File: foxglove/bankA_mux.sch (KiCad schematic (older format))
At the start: 6 parts, among them U10 SHIFTER, U9 74HC4051

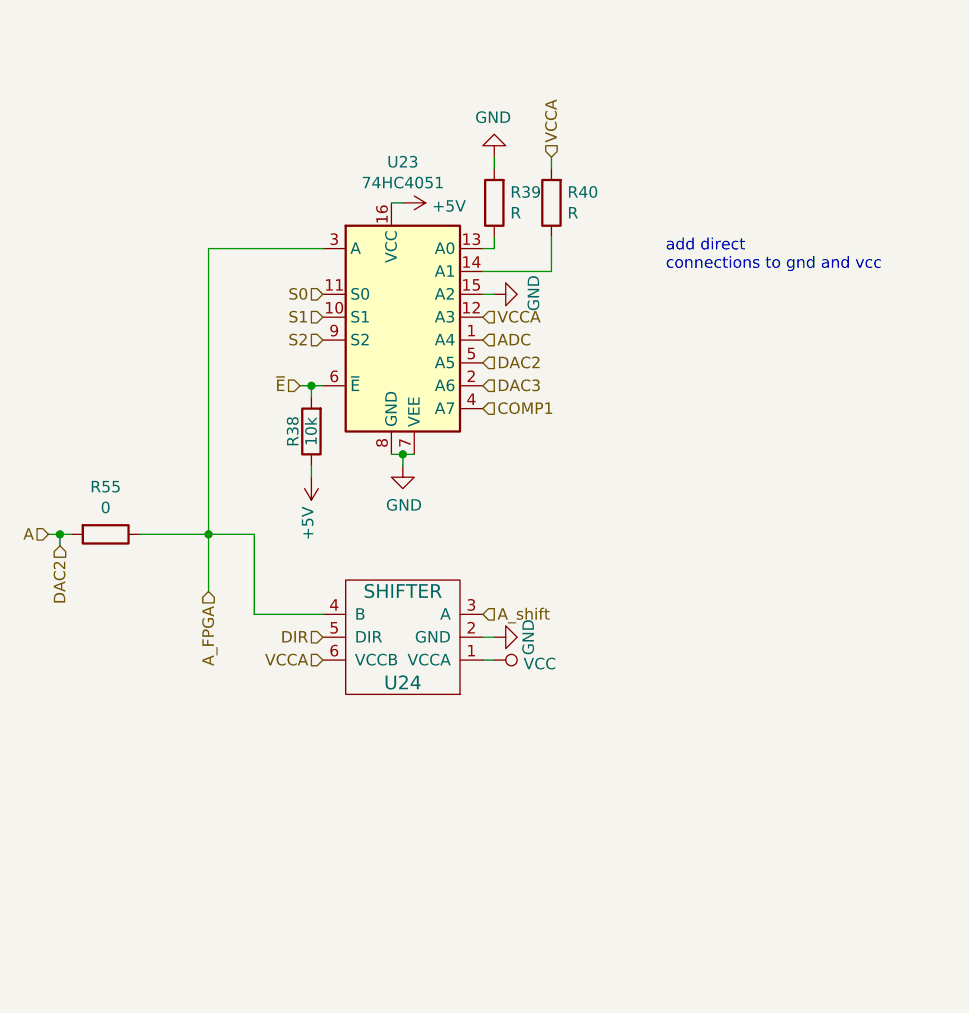
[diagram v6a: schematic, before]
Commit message: Made FPGA connections to greatfet headers
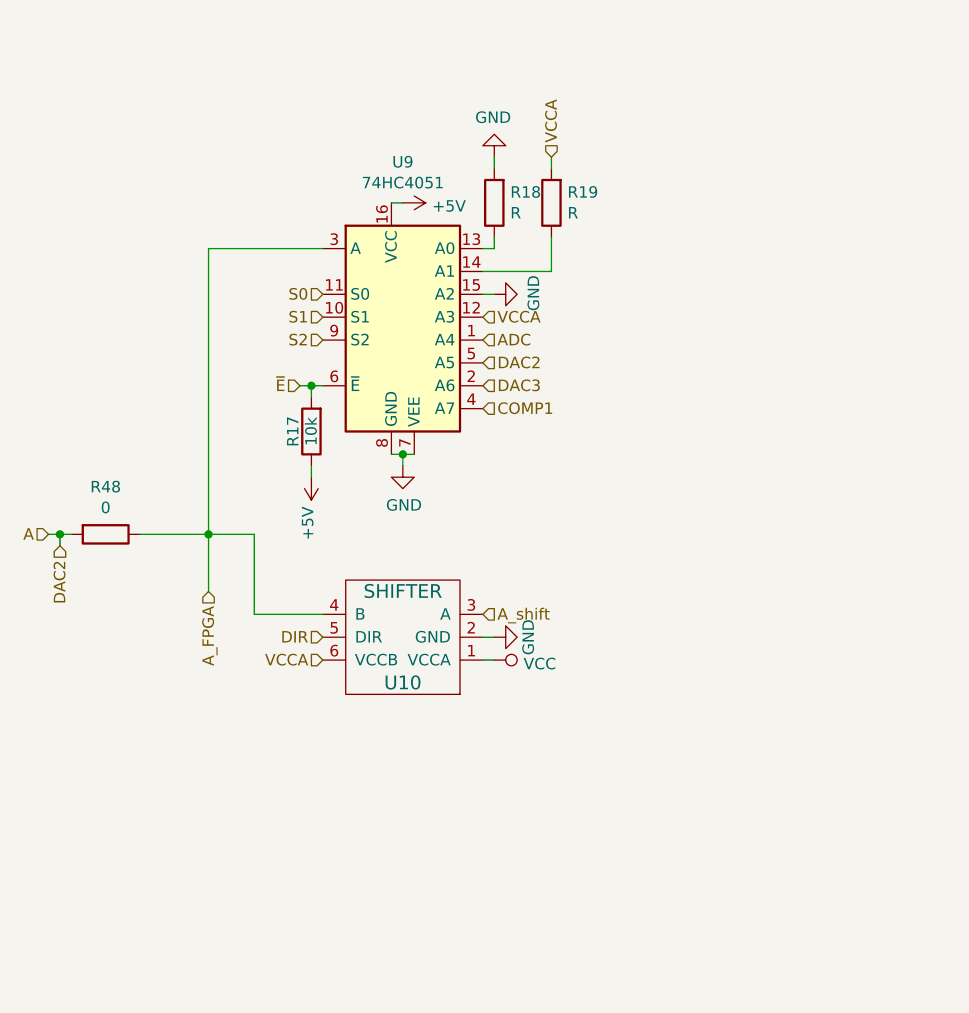
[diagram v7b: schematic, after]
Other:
- note removed: "add direct\nconnections to gnd and vcc"
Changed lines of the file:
@@
 AR Path="/5D1A4680/5CF3E254" Ref="U21"  Part="1"
 AR Path="/5D1A4696/5CF3E254" Ref="U23"  Part="1"
-F 0 "U23" H 4100 3428 50  0000 C CNN
+F 0 "U9" H 4100 3428 50  0000 C CNN
 F 1 "74HC4051" H 4100 3337 50  0000 C CNN
 F 2 "Package_TO_SOT_SMD:SOT-763-1" H 4050 2350 50  0001 C CNN
@@
 AR Path="/5D1A4680/5CF3E25C" Ref="#PWR0180"  Part="1"
 AR Path="/5D1A4696/5CF3E25C" Ref="#PWR0186"  Part="1"
-F 0 "#PWR0186" H 4100 2100 50  0001 C CNN
+F 0 "#PWR0144" H 4100 2100 50  0001 C CNN
 F 1 "+5V" V 4115 2378 50  0000 L CNN
 F 2 "" H 4100 2250 50  0001 C CNN
@@
 AR Path="/5D1A4680/5CF3E263" Ref="#PWR0181"  Part="1"
 AR Path="/5D1A4696/5CF3E263" Ref="#PWR0187"  Part="1"
-F 0 "#PWR0187" H 4100 3150 50  0001 C CNN
+F 0 "#PWR0145" H 4100 3150 50  0001 C CNN
 F 1 "GND" H 4105 3227 50  0000 C CNN
 F 2 "" H 4100 3400 50  0001 C CNN
@@
 AR Path="/5D1A4680/5CF3E26E" Ref="R36"  Part="1"
 AR Path="/5D1A4696/5CF3E26E" Ref="R39"  Part="1"
-F 0 "R39" H 4430 2204 50  0000 R CNN
+F 0 "R18" H 4430 2204 50  0000 R CNN
 F 1 "R" H 4430 2295 50  0000 R CNN
 F 2 "gsg-modules:0402" V 4430 2250 50  0001 C CNN
@@
 AR Path="/5D1A4680/5CF3E275" Ref="R37"  Part="1"
 AR Path="/5D1A4696/5CF3E275" Ref="R40"  Part="1"
-F 0 "R40" H 4680 2204 50  0000 R CNN
+F 0 "R19" H 4680 2204 50  0000 R CNN
 F 1 "R" H 4680 2295 50  0000 R CNN
 F 2 "gsg-modules:0402" V 4680 2250 50  0001 C CNN
@@
 AR Path="/5D1A4680/5CF3E282" Ref="#PWR0182"  Part="1"
 AR Path="/5D1A4696/5CF3E282" Ref="#PWR0188"  Part="1"
-F 0 "#PWR0188" H 4500 1800 50  0001 C CNN
+F 0 "#PWR0146" H 4500 1800 50  0001 C CNN
 F 1 "GND" H 4505 1877 50  0000 C CNN
 F 2 "" H 4500 2050 50  0001 C CNN
@@
 AR Path="/5D1A4680/5CF3E28C" Ref="U22"  Part="1"
 AR Path="/5D1A4696/5CF3E28C" Ref="U24"  Part="1"
-F 0 "U24" H 4100 4350 60  0000 C CNN
+F 0 "U10" H 4100 4350 60  0000 C CNN
 F 1 "SHIFTER" H 4100 3950 60  0000 C CNN
 F 2 "gsg-modules:SOT363" H 4100 4150 60  0001 C CNN
@@
 AR Path="/5D1A4680/5CF3E293" Ref="#PWR0183"  Part="1"
 AR Path="/5D1A4696/5CF3E293" Ref="#PWR0189"  Part="1"
-F 0 "#PWR0189" H 4500 3900 50  0001 C CNN
+F 0 "#PWR0147" H 4500 3900 50  0001 C CNN
 F 1 "GND" H 4500 4000 50  0000 C CNN
 F 2 "" H 4500 4150 60  0000 C CNN
@@
 AR Path="/5D1A4680/5CF3E2A6" Ref="R35"  Part="1"
 AR Path="/5D1A4696/5CF3E2A6" Ref="R38"  Part="1"
-F 0 "R38" V 3780 3250 50  0000 C CNN
+F 0 "R17" V 3780 3250 50  0000 C CNN
 F 1 "10k" V 3700 3250 50  0000 C CNN
 F 2 "gsg-modules:0402" V 3630 3250 50  0001 C CNN
@@
 AR Path="/5D1A4680/5CF3E2B2" Ref="#PWR0184"  Part="1"
 AR Path="/5D1A4696/5CF3E2B2" Ref="#PWR0190"  Part="1"
-F 0 "#PWR0190" H 3700 3300 50  0001 C CNN
+F 0 "#PWR0148" H 3700 3300 50  0001 C CNN
 F 1 "+5V" V 3715 3578 50  0000 L CNN
 F 2 "" H 3700 3450 50  0001 C CNN
@@
 AR Path="/5D1A4680/5CF3E2B8" Ref="#PWR0185"  Part="1"
 AR Path="/5D1A4696/5CF3E2B8" Ref="#PWR0191"  Part="1"
-F 0 "#PWR0191" H 4500 4100 50  0001 C CNN
+F 0 "#PWR0149" H 4500 4100 50  0001 C CNN
 F 1 "VCC" V 4517 4378 50  0000 L CNN
 F 2 "" H 4500 4250 50  0001 C CNN
@@
 AR Path="/5D190D22/5CB0C423" Ref="R51"  Part="1"
 AR Path="/5D1A466A/5CB0C423" Ref="R53"  Part="1"
-F 0 "R55" V 2593 3700 50  0000 C CNN
+F 0 "R48" V 2593 3700 50  0000 C CNN
 F 1 "0" V 2684 3700 50  0000 C CNN
 F 2 "gsg-modules:0402" V 2730 3700 50  0001 C CNN
@@
 Wire Wire Line
 	2950 3700 3250 3700
-Text Notes 5250 2550 0    50   ~ 0
-add direct\nconnections to gnd and vcc
 $Comp
 L power:GND #PWR?
@@
 AR Path="/5D1A4680/5CCD056F" Ref="#PWR0238"  Part="1"
 AR Path="/5D1A4696/5CCD056F" Ref="#PWR0239"  Part="1"
-F 0 "#PWR0239" H 4500 2400 50  0001 C CNN
+F 0 "#PWR0232" H 4500 2400 50  0001 C CNN
 F 1 "GND" H 4505 2477 50  0000 C CNN
 F 2 "" H 4500 2650 50  0001 C CNN

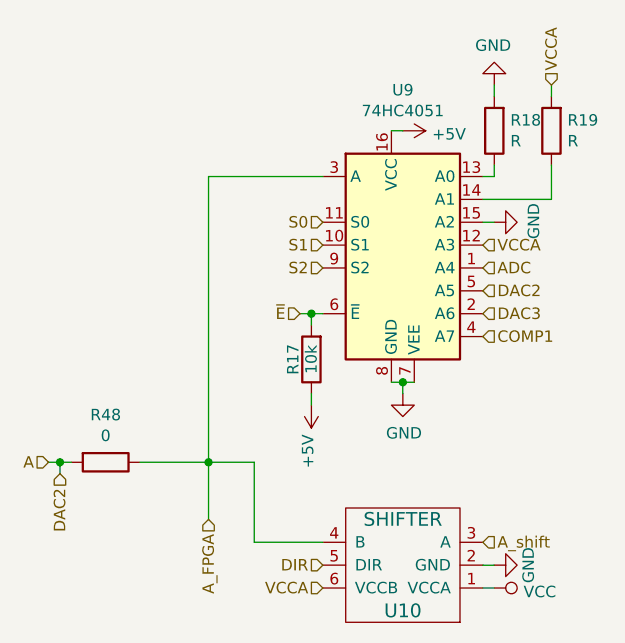
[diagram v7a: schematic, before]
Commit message: Started routing connections to J2 and J7
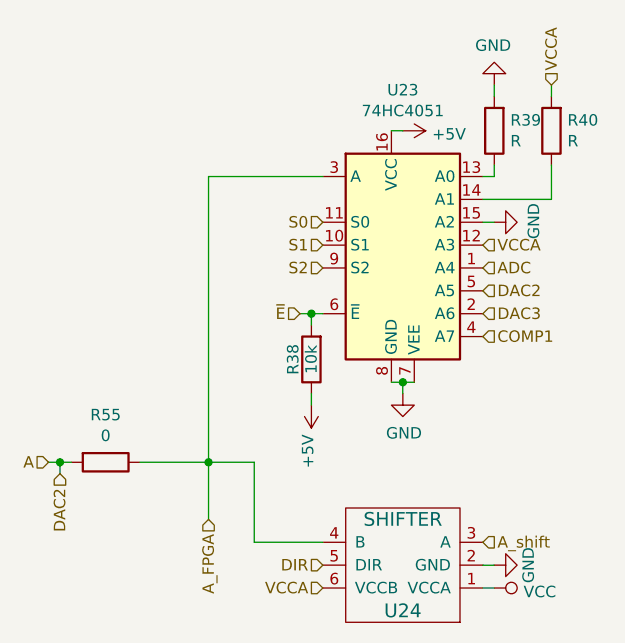
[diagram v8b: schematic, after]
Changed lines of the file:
@@
 $Descr A4 11693 8268
 encoding utf-8
-Sheet 2 9
+Sheet 9 9
 Title ""
 Date ""
@@
 AR Path="/5D1A4680/5CF3E254" Ref="U21"  Part="1"
 AR Path="/5D1A4696/5CF3E254" Ref="U23"  Part="1"
-F 0 "U9" H 4100 3428 50  0000 C CNN
+F 0 "U23" H 4100 3428 50  0000 C CNN
 F 1 "74HC4051" H 4100 3337 50  0000 C CNN
 F 2 "Package_TO_SOT_SMD:SOT-763-1" H 4050 2350 50  0001 C CNN
@@
 AR Path="/5D1A4680/5CF3E25C" Ref="#PWR0180"  Part="1"
 AR Path="/5D1A4696/5CF3E25C" Ref="#PWR0186"  Part="1"
-F 0 "#PWR0144" H 4100 2100 50  0001 C CNN
+F 0 "#PWR0186" H 4100 2100 50  0001 C CNN
 F 1 "+5V" V 4115 2378 50  0000 L CNN
 F 2 "" H 4100 2250 50  0001 C CNN
@@
 AR Path="/5D1A4680/5CF3E263" Ref="#PWR0181"  Part="1"
 AR Path="/5D1A4696/5CF3E263" Ref="#PWR0187"  Part="1"
-F 0 "#PWR0145" H 4100 3150 50  0001 C CNN
+F 0 "#PWR0187" H 4100 3150 50  0001 C CNN
 F 1 "GND" H 4105 3227 50  0000 C CNN
 F 2 "" H 4100 3400 50  0001 C CNN
@@
 AR Path="/5D1A4680/5CF3E26E" Ref="R36"  Part="1"
 AR Path="/5D1A4696/5CF3E26E" Ref="R39"  Part="1"
-F 0 "R18" H 4430 2204 50  0000 R CNN
+F 0 "R39" H 4430 2204 50  0000 R CNN
 F 1 "R" H 4430 2295 50  0000 R CNN
 F 2 "gsg-modules:0402" V 4430 2250 50  0001 C CNN
@@
 AR Path="/5D1A4680/5CF3E275" Ref="R37"  Part="1"
 AR Path="/5D1A4696/5CF3E275" Ref="R40"  Part="1"
-F 0 "R19" H 4680 2204 50  0000 R CNN
+F 0 "R40" H 4680 2204 50  0000 R CNN
 F 1 "R" H 4680 2295 50  0000 R CNN
 F 2 "gsg-modules:0402" V 4680 2250 50  0001 C CNN
@@
 AR Path="/5D1A4680/5CF3E282" Ref="#PWR0182"  Part="1"
 AR Path="/5D1A4696/5CF3E282" Ref="#PWR0188"  Part="1"
-F 0 "#PWR0146" H 4500 1800 50  0001 C CNN
+F 0 "#PWR0188" H 4500 1800 50  0001 C CNN
 F 1 "GND" H 4505 1877 50  0000 C CNN
 F 2 "" H 4500 2050 50  0001 C CNN
@@
 AR Path="/5D1A4680/5CF3E28C" Ref="U22"  Part="1"
 AR Path="/5D1A4696/5CF3E28C" Ref="U24"  Part="1"
-F 0 "U10" H 4100 4350 60  0000 C CNN
+F 0 "U24" H 4100 4350 60  0000 C CNN
 F 1 "SHIFTER" H 4100 3950 60  0000 C CNN
 F 2 "gsg-modules:SOT363" H 4100 4150 60  0001 C CNN
@@
 AR Path="/5D1A4680/5CF3E293" Ref="#PWR0183"  Part="1"
 AR Path="/5D1A4696/5CF3E293" Ref="#PWR0189"  Part="1"
-F 0 "#PWR0147" H 4500 3900 50  0001 C CNN
+F 0 "#PWR0189" H 4500 3900 50  0001 C CNN
 F 1 "GND" H 4500 4000 50  0000 C CNN
 F 2 "" H 4500 4150 60  0000 C CNN
@@
 AR Path="/5D1A4680/5CF3E2A6" Ref="R35"  Part="1"
 AR Path="/5D1A4696/5CF3E2A6" Ref="R38"  Part="1"
-F 0 "R17" V 3780 3250 50  0000 C CNN
+F 0 "R38" V 3780 3250 50  0000 C CNN
 F 1 "10k" V 3700 3250 50  0000 C CNN
 F 2 "gsg-modules:0402" V 3630 3250 50  0001 C CNN
@@
 AR Path="/5D1A4680/5CF3E2B2" Ref="#PWR0184"  Part="1"
 AR Path="/5D1A4696/5CF3E2B2" Ref="#PWR0190"  Part="1"
-F 0 "#PWR0148" H 3700 3300 50  0001 C CNN
+F 0 "#PWR0190" H 3700 3300 50  0001 C CNN
 F 1 "+5V" V 3715 3578 50  0000 L CNN
 F 2 "" H 3700 3450 50  0001 C CNN
@@
 AR Path="/5D1A4680/5CF3E2B8" Ref="#PWR0185"  Part="1"
 AR Path="/5D1A4696/5CF3E2B8" Ref="#PWR0191"  Part="1"
-F 0 "#PWR0149" H 4500 4100 50  0001 C CNN
+F 0 "#PWR0191" H 4500 4100 50  0001 C CNN
 F 1 "VCC" V 4517 4378 50  0000 L CNN
 F 2 "" H 4500 4250 50  0001 C CNN
@@
 AR Path="/5D190D22/5CB0C423" Ref="R51"  Part="1"
 AR Path="/5D1A466A/5CB0C423" Ref="R53"  Part="1"
-F 0 "R48" V 2593 3700 50  0000 C CNN
+F 0 "R55" V 2593 3700 50  0000 C CNN
 F 1 "0" V 2684 3700 50  0000 C CNN
 F 2 "gsg-modules:0402" V 2730 3700 50  0001 C CNN
@@
 AR Path="/5D1A4680/5CCD056F" Ref="#PWR0238"  Part="1"
 AR Path="/5D1A4696/5CCD056F" Ref="#PWR0239"  Part="1"
-F 0 "#PWR0232" H 4500 2400 50  0001 C CNN
+F 0 "#PWR0239" H 4500 2400 50  0001 C CNN
 F 1 "GND" H 4505 2477 50  0000 C CNN
 F 2 "" H 4500 2650 50  0001 C CNN
